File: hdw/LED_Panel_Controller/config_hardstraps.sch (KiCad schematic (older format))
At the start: 19 parts

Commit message: added digikey pns, footprints, bom scrubbed
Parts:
- C?: Digi-Key PN (none) -> 490-10701-1-ND
- J? (x3): footprint (none) -> Connector_PinHeader_2.54mm:PinHeader_1x03_P2.54mm_Vertical; Configuration (none) -> DNP
- J? (x3): footprint (none) -> Connector_PinHeader_2.54mm:PinHeader_1x04_P2.54mm_Vertical; Configuration (none) -> DNP
- R? (x5): Digi-Key PN (none) -> RMCF0402FT10K0CT-ND
- R? (x5): Digi-Key PN (none) -> RMCF0402FT10R0CT-ND
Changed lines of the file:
@@
 F 5 "1%" H 2980 2200 50  0000 L CNN "Tolerance"
 F 6 "1/16W" H 2980 2100 50  0000 L CNN "Wattage"
-F 7 "" H 3180 2630 60  0001 C CNN "Digi-Key PN"
+F 7 "RMCF0402FT10K0CT-ND" H 3180 2630 60  0001 C CNN "Digi-Key PN"
 	1    2880 2230
 	-1   0    0    -1
@@
 F 6 "1/16W" H 2980 2560 50  0000 L CNN "Wattage"
 F 7 "Telemetry" H 2610 2600 50  0000 C CNN "Configuration"
+F 8 "RMCF0402FT10R0CT-ND" H 2880 2690 50  0001 C CNN "Digi-Key PN"
 	1    2880 2690
 	-1   0    0    -1
@@
 F 5 "1%" H 4540 2200 50  0000 L CNN "Tolerance"
 F 6 "1/16W" H 4540 2100 50  0000 L CNN "Wattage"
-F 7 "" H 4740 2630 60  0001 C CNN "Digi-Key PN"
+F 7 "RMCF0402FT10K0CT-ND" H 4740 2630 60  0001 C CNN "Digi-Key PN"
 	1    4440 2230
 	-1   0    0    -1
@@
 F 6 "1/16W" H 4540 2560 50  0000 L CNN "Wattage"
 F 7 "ETC" H 4280 2600 50  0000 C CNN "Configuration"
+F 8 "RMCF0402FT10R0CT-ND" H 4440 2690 50  0001 C CNN "Digi-Key PN"
 	1    4440 2690
 	-1   0    0    -1
@@
 F 5 "1%" H 6100 2200 50  0000 L CNN "Tolerance"
 F 6 "1/16W" H 6100 2100 50  0000 L CNN "Wattage"
-F 7 "" H 6300 2630 60  0001 C CNN "Digi-Key PN"
+F 7 "RMCF0402FT10K0CT-ND" H 6300 2630 60  0001 C CNN "Digi-Key PN"
 	1    6000 2230
 	-1   0    0    -1
@@
 F 6 "1/16W" H 6100 2560 50  0000 L CNN "Wattage"
 F 7 "WIFI" H 5840 2600 50  0000 C CNN "Configuration"
+F 8 "RMCF0402FT10R0CT-ND" H 6000 2690 50  0001 C CNN "Digi-Key PN"
 	1    6000 2690
 	-1   0    0    -1
@@
 F 5 "1%" H 7350 2200 50  0000 L CNN "Tolerance"
 F 6 "1/16W" H 7350 2100 50  0000 L CNN "Wattage"
-F 7 "" H 7550 2630 60  0001 C CNN "Digi-Key PN"
+F 7 "RMCF0402FT10K0CT-ND" H 7550 2630 60  0001 C CNN "Digi-Key PN"
 	1    7250 2230
 	-1   0    0    -1
@@
 F 6 "1/16W" H 7350 2560 50  0000 L CNN "Wattage"
 F 7 "BACKUP_RTC" H 7160 2600 50  0000 R CNN "Configuration"
+F 8 "RMCF0402FT10R0CT-ND" H 7250 2690 50  0001 C CNN "Digi-Key PN"
 	1    7250 2690
 	-1   0    0    -1
@@
 F 5 "1%" H 2980 3410 50  0000 L CNN "Tolerance"
 F 6 "1/16W" H 2980 3310 50  0000 L CNN "Wattage"
-F 7 "" H 3180 3840 60  0001 C CNN "Digi-Key PN"
+F 7 "RMCF0402FT10K0CT-ND" H 3180 3840 60  0001 C CNN "Digi-Key PN"
 	1    2880 3440
 	-1   0    0    -1
@@
 F 6 "1/16W" H 2980 3770 50  0000 L CNN "Wattage"
 F 7 "SPI_FLASH" H 2610 3810 50  0000 C CNN "Configuration"
+F 8 "RMCF0402FT10R0CT-ND" H 2880 3900 50  0001 C CNN "Digi-Key PN"
 	1    2880 3900
 	-1   0    0    -1
@@
 F 6 "X7R" H 2370 6950 50  0000 R CNN "Dielectric"
 F 7 "Telemetry" H 2370 7240 50  0000 R CNN "Configuration"
+F 8 "490-10701-1-ND" H 2520 7090 50  0001 C CNN "Digi-Key PN"
 	1    2520 7090
 	1    0    0    -1
@@
 F 0 "J?" H 6020 5220 50  0000 C CNN
 F 1 "I2C" H 6020 4820 50  0000 C CNN
-F 2 "" H 6020 5020 50  0001 C CNN
+F 2 "Connector_PinHeader_2.54mm:PinHeader_1x03_P2.54mm_Vertical" H 6020 5020 50  0001 C CNN
 F 3 "~" H 6020 5020 50  0001 C CNN
+F 4 "DNP" H 6020 5020 50  0001 C CNN "Configuration"
 	1    6020 5020
 	1    0    0    -1
@@
 F 0 "J?" H 7020 5220 50  0000 C CNN
 F 1 "WIFI_SPI" H 7020 4720 50  0000 C CNN
-F 2 "" H 7020 5020 50  0001 C CNN
+F 2 "Connector_PinHeader_2.54mm:PinHeader_1x04_P2.54mm_Vertical" H 7020 5020 50  0001 C CNN
 F 3 "~" H 7020 5020 50  0001 C CNN
+F 4 "DNP" H 7020 5020 50  0001 C CNN "Configuration"
 	1    7020 5020
 	1    0    0    -1
@@
 F 0 "J?" H 8020 5220 50  0000 C CNN
 F 1 "SD_SPI" H 8020 4720 50  0000 C CNN
-F 2 "" H 8020 5020 50  0001 C CNN
+F 2 "Connector_PinHeader_2.54mm:PinHeader_1x04_P2.54mm_Vertical" H 8020 5020 50  0001 C CNN
 F 3 "~" H 8020 5020 50  0001 C CNN
+F 4 "DNP" H 8020 5020 50  0001 C CNN "Configuration"
 	1    8020 5020
 	1    0    0    -1
@@
 F 0 "J?" H 9020 5220 50  0000 C CNN
 F 1 "FLASH_SPI" H 9020 4720 50  0000 C CNN
-F 2 "" H 9020 5020 50  0001 C CNN
+F 2 "Connector_PinHeader_2.54mm:PinHeader_1x04_P2.54mm_Vertical" H 9020 5020 50  0001 C CNN
 F 3 "~" H 9020 5020 50  0001 C CNN
+F 4 "DNP" H 9020 5020 50  0001 C CNN "Configuration"
 	1    9020 5020
 	1    0    0    -1
@@
 F 0 "J?" H 5020 5220 50  0000 C CNN
 F 1 "PIC_UART" H 5020 4820 50  0000 C CNN
-F 2 "" H 5020 5020 50  0001 C CNN
+F 2 "Connector_PinHeader_2.54mm:PinHeader_1x03_P2.54mm_Vertical" H 5020 5020 50  0001 C CNN
 F 3 "~" H 5020 5020 50  0001 C CNN
+F 4 "DNP" H 5020 5020 50  0001 C CNN "Configuration"
 	1    5020 5020
 	1    0    0    -1
@@
 F 0 "J?" H 5020 5970 50  0000 C CNN
 F 1 "WIFI_UART" H 5020 5570 50  0000 C CNN
-F 2 "" H 5020 5770 50  0001 C CNN
+F 2 "Connector_PinHeader_2.54mm:PinHeader_1x03_P2.54mm_Vertical" H 5020 5770 50  0001 C CNN
 F 3 "~" H 5020 5770 50  0001 C CNN
+F 4 "DNP" H 5020 5770 50  0001 C CNN "Configuration"
 	1    5020 5770
 	1    0    0    -1

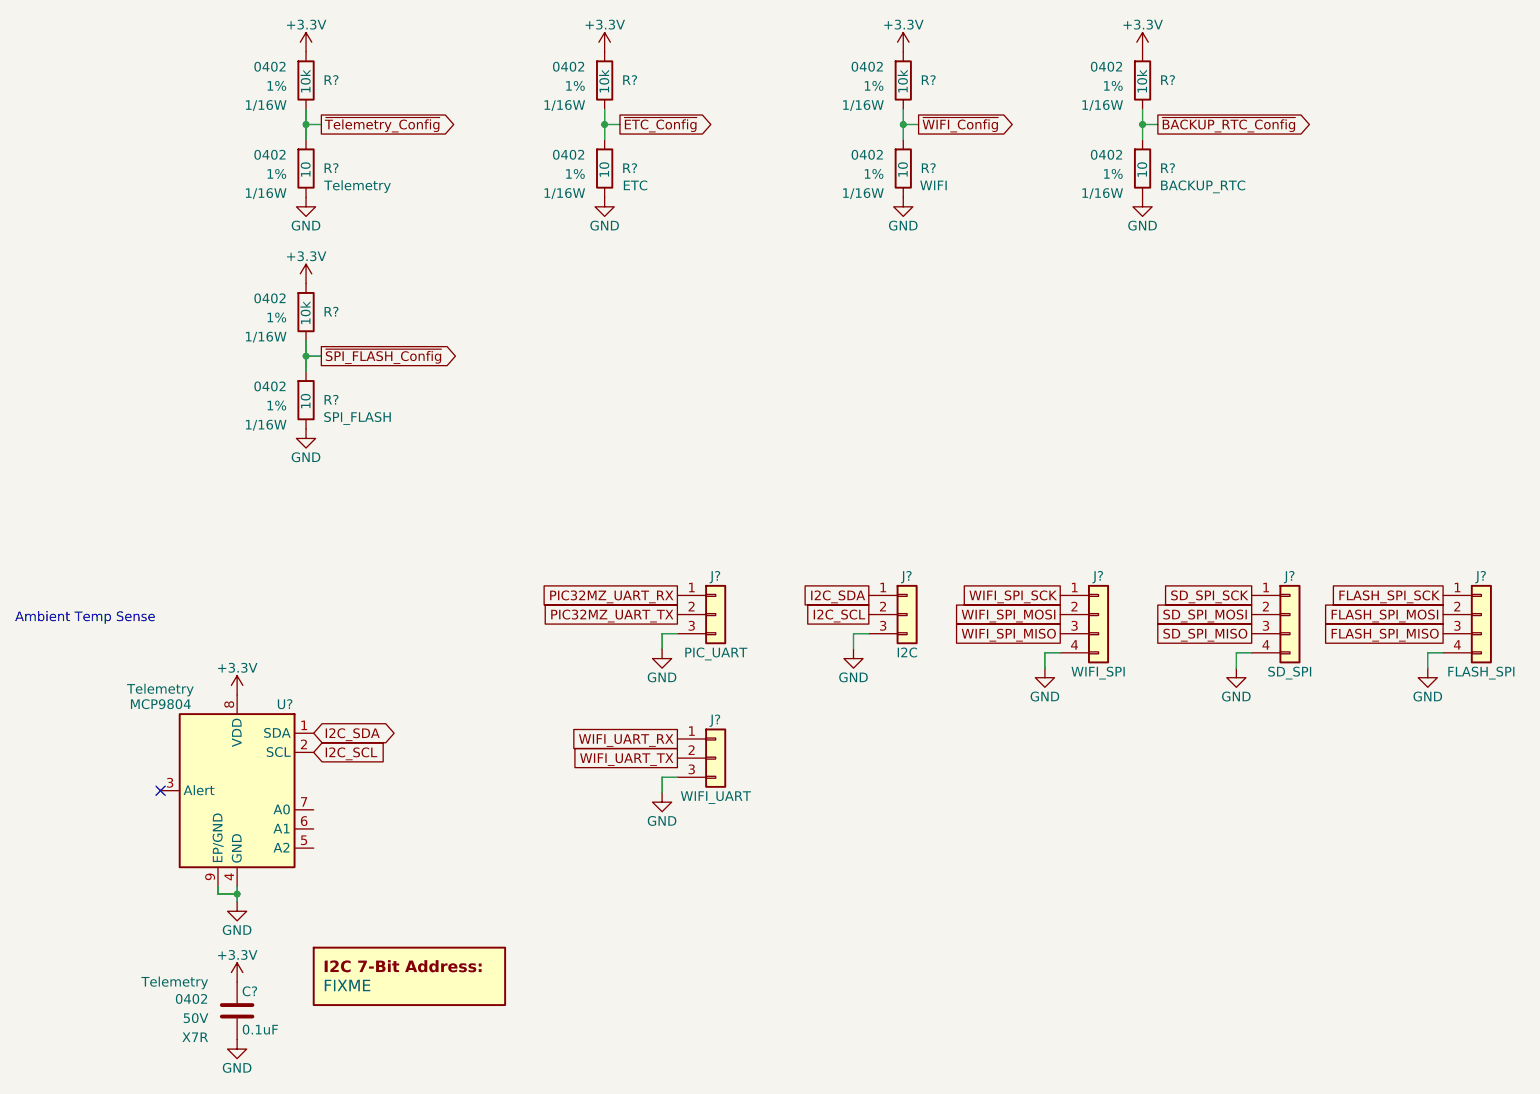
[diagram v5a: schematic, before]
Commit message: assigned I2C addresses
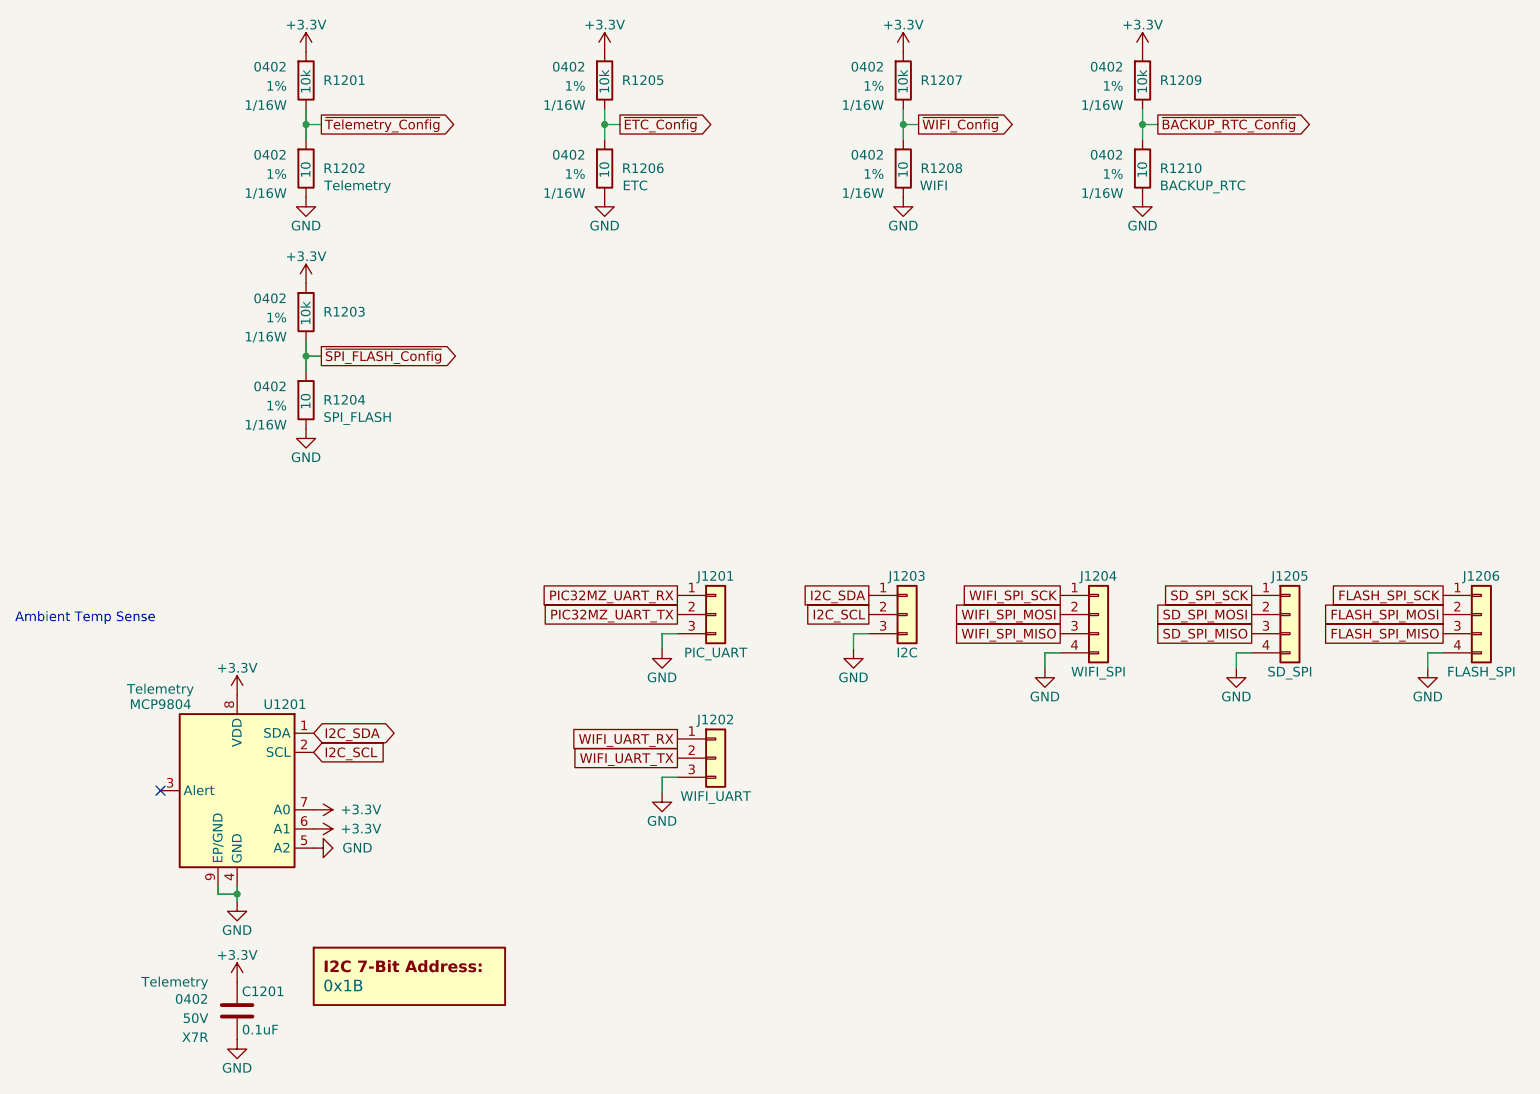
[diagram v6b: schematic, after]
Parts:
- DOC1201: renamed from DOC?; value FIXME -> 0x1B
- gave numbers to parts that had none: 18
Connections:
- net +3V3: now also U1201.6 (A1), U1201.7 (A0)
- net GND: now also U1201.5 (A2)
